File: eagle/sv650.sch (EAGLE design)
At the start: 18 parts, among them IC1 7805

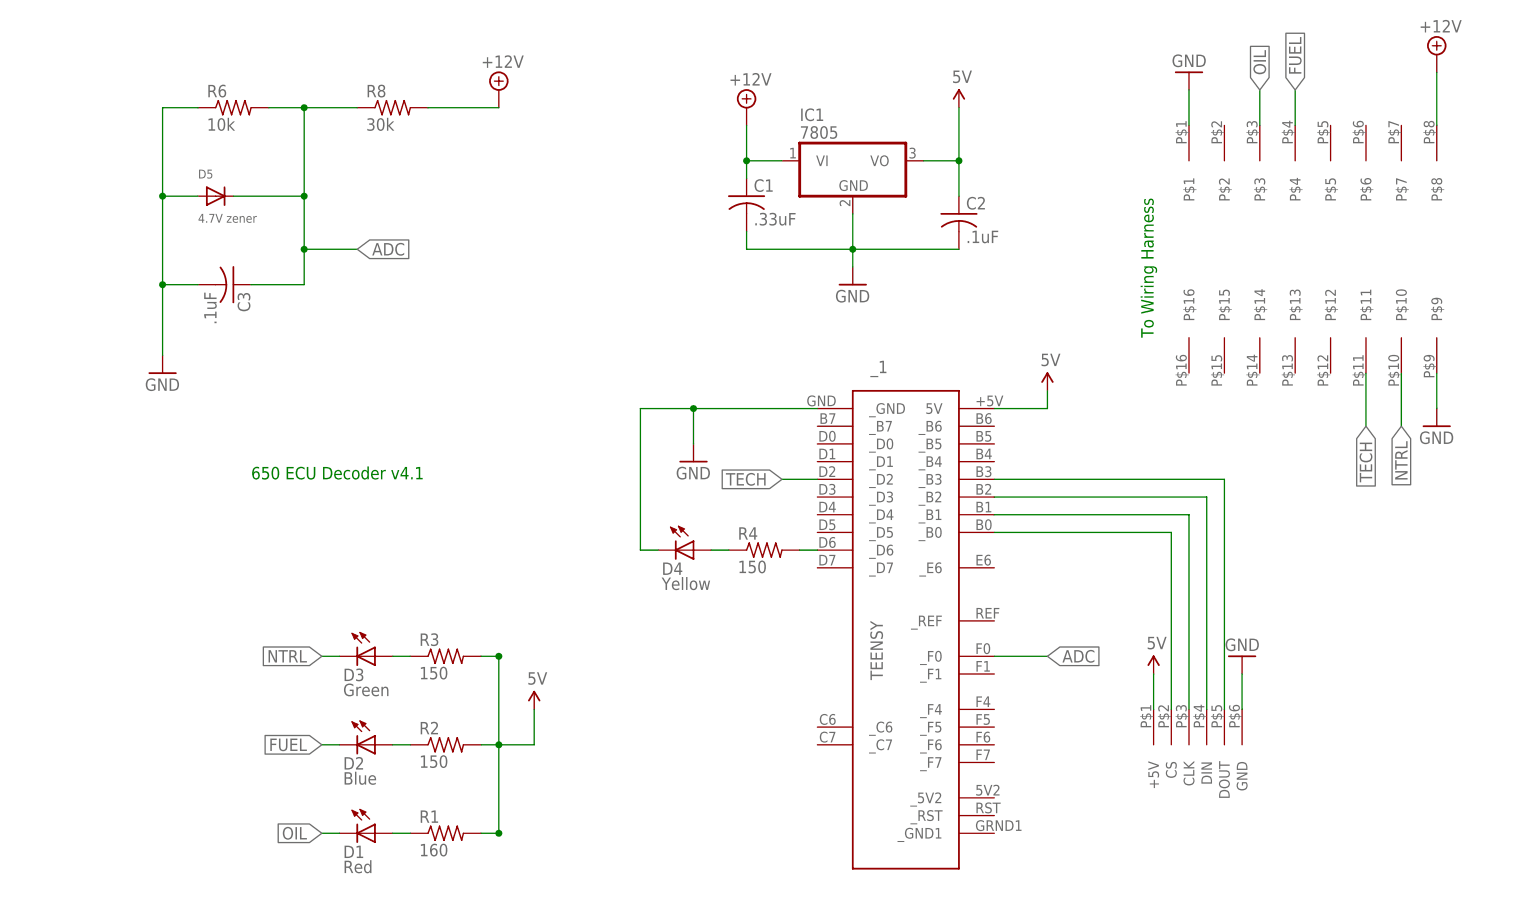
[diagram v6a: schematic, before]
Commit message: Add 'mode' button Add means to detect Very Low Fuel on later models Move +12V back to ignition
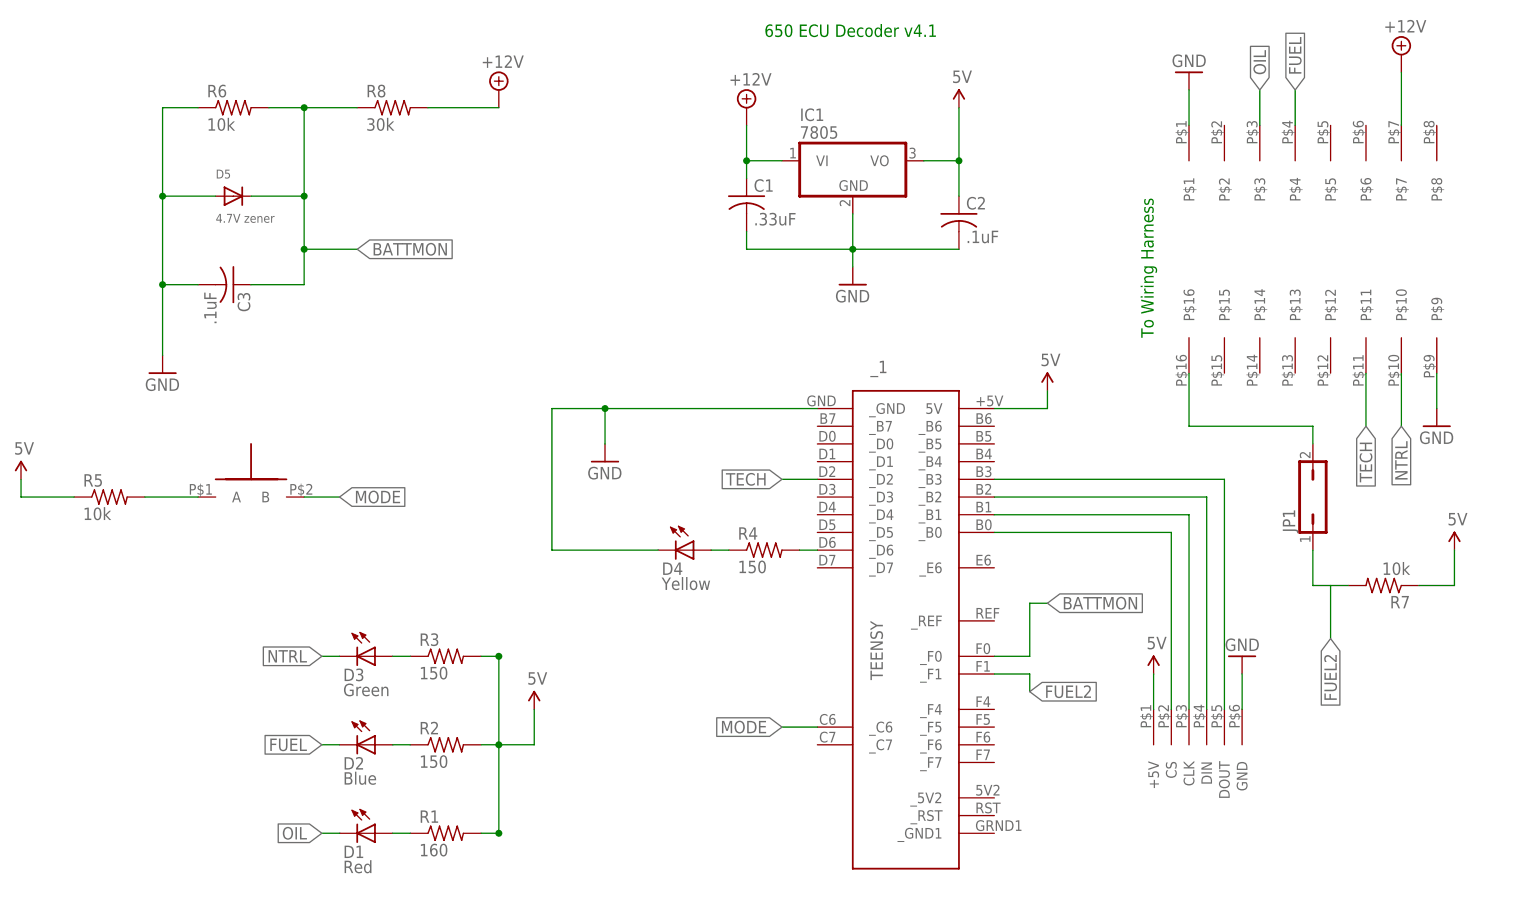
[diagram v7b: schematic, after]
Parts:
- added JP1: (no value), jumper:JP1Q
- added R5, R7: 10k, resistor:R-US_M0805
- added U$10: R13-509A-05-BB/R13-509A-05-BR, synfinatic:R13-509A-05-BB/R13-509A-05-BR
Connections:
- net ADC renamed BATTMON
- new net FUEL2: JP1.1, R7.2, _1._F1
- new net LOWFUEL2: JP1.2, U$3.P$16
- new net MODE: U$10.B, _1._C6
- new net N$12: R5.2, U$10.A
- net +12V: now also U$3.P$7; no longer U$3.P$8
- net 5V: now also R5.1, R7.1
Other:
- moved on the sheet: D5
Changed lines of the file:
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@@
 <attribute name="OC_NEWARK" value="05F1511"/>
 </part>
-<part name="SUPPLY3" library="supply2" deviceset="+12V" device=""/>
 <part name="GND2" library="SparkFun" deviceset="GND" device=""/>
 <part name="C3" library="adafruit" deviceset="C-US" device="025-024X044" value=".1uF">
@@
 <attribute name="OC_NEWARK" value="35K8677"/>
 </part>
+<part name="R5" library="resistor" deviceset="R-US_" device="M0805" value="10k">
+<attribute name="MF" value="VISHAY/DALE"/>
+<attribute name="MPN" value="CRCW080510K0FKTA"/>
+<attribute name="OC_NEWARK" value="05F1511"/>
+</part>
+<part name="U$11" library="SparkFun" deviceset="5V" device=""/>
+<part name="U$10" library="synfinatic" deviceset="R13-509A-05-BB/R13-509A-05-BR" device=""/>
+<part name="SUPPLY4" library="supply2" deviceset="+12V" device=""/>
+<part name="JP1" library="jumper" deviceset="JP1Q" device=""/>
+<part name="R7" library="resistor" deviceset="R-US_" device="M0805" value="10k">
+<attribute name="MF" value="VISHAY/DALE"/>
+<attribute name="MPN" value="CRCW080510K0FKTA"/>
+<attribute name="OC_NEWARK" value="05F1511"/>
+</part>
+<part name="U$12" library="SparkFun" deviceset="5V" device=""/>
 </parts>
 <sheets>
@@
 <plain>
 <text x="114.3" y="68.58" size="1.778" layer="91" rot="R90">To Wiring Harness</text>
-<text x="-15.24" y="48.26" size="1.778" layer="91">650 ECU Decoder v4.1</text>
+<text x="58.42" y="111.76" size="1.778" layer="91">650 ECU Decoder v4.1</text>
 </plain>
 <instances>
@@
 <instance part="GND6" gate="1" x="127" y="22.86" rot="R180"/>
 <instance part="U$9" gate="G$1" x="25.4" y="15.24"/>
-<instance part="GND1" gate="1" x="48.26" y="50.8"/>
+<instance part="GND1" gate="1" x="35.56" y="50.8"/>
 <instance part="SUPPLY1" gate="+12V" x="20.32" y="104.14"/>
 <instance part="SUPPLY2" gate="+12V" x="55.88" y="101.6"/>
@@
 <attribute name="MPN" x="5.08" y="101.6" size="1.778" layer="96" display="off"/>
 </instance>
-<instance part="SUPPLY3" gate="+12V" x="154.94" y="109.22"/>
 <instance part="GND2" gate="1" x="-27.94" y="63.5"/>
 <instance part="C3" gate="G$1" x="-17.78" y="76.2" rot="R270">
@@
 <attribute name="MPN" x="-17.78" y="76.2" size="1.778" layer="96" rot="R270" display="off"/>
 </instance>
-<instance part="D5" gate="G$1" x="-20.32" y="88.9">
-<attribute name="OC_NEWARK" x="-20.32" y="88.9" size="1.778" layer="96" rot="R270" display="off"/>
-<attribute name="MF" x="-20.32" y="88.9" size="1.778" layer="96" rot="R270" display="off"/>
-<attribute name="MPN" x="-20.32" y="88.9" size="1.778" layer="96" rot="R270" display="off"/>
-</instance>
+<instance part="D5" gate="G$1" x="-17.78" y="88.9">
+<attribute name="OC_NEWARK" x="-17.78" y="88.9" size="1.778" layer="96" rot="R270" display="off"/>
+<attribute name="MF" x="-17.78" y="88.9" size="1.778" layer="96" rot="R270" display="off"/>
+<attribute name="MPN" x="-17.78" y="88.9" size="1.778" layer="96" rot="R270" display="off"/>
+</instance>
+<instance part="R5" gate="G$1" x="-35.56" y="45.72">
+<attribute name="OC_NEWARK" x="-35.56" y="45.72" size="1.778" layer="96" display="off"/>
+<attribute name="MF" x="-35.56" y="45.72" size="1.778" layer="96" display="off"/>
+<attribute name="MPN" x="-35.56" y="45.72" size="1.778" layer="96" display="off"/>
+</instance>
+<instance part="U$11" gate="G$1" x="-48.26" y="48.26"/>
+<instance part="U$10" gate="G$1" x="-20.32" y="43.18"/>
+<instance part="SUPPLY4" gate="+12V" x="149.86" y="109.22"/>
+<instance part="JP1" gate="A" x="137.16" y="45.72"/>
+<instance part="R7" gate="G$1" x="147.32" y="33.02" rot="R180">
+<attribute name="OC_NEWARK" x="147.32" y="33.02" size="1.778" layer="96" rot="R180" display="off"/>
+<attribute name="MF" x="147.32" y="33.02" size="1.778" layer="96" rot="R180" display="off"/>
+<attribute name="MPN" x="147.32" y="33.02" size="1.778" layer="96" rot="R180" display="off"/>
+</instance>
+<instance part="U$12" gate="G$1" x="157.48" y="38.1"/>
 </instances>
 <busses>
@@
 <wire x1="114.3" y1="20.32" x2="114.3" y2="15.24" width="0.1524" layer="91"/>
 </segment>
+<segment>
+<pinref part="R5" gate="G$1" pin="1"/>
+<wire x1="-40.64" y1="45.72" x2="-48.26" y2="45.72" width="0.1524" layer="91"/>
+<pinref part="U$11" gate="G$1" pin="5V"/>
+<wire x1="-48.26" y1="45.72" x2="-48.26" y2="48.26" width="0.1524" layer="91"/>
+</segment>
+<segment>
+<pinref part="R7" gate="G$1" pin="1"/>
+<wire x1="152.4" y1="33.02" x2="157.48" y2="33.02" width="0.1524" layer="91"/>
+<wire x1="157.48" y1="33.02" x2="157.48" y2="38.1" width="0.1524" layer="91"/>
+<pinref part="U$12" gate="G$1" pin="5V"/>
+</segment>
 </net>
 <net name="GND" class="0">
@@
 <pinref part="_1" gate="G$1" pin="_GND"/>
 <pinref part="D4" gate="G$1" pin="C"/>
-<wire x1="43.18" y1="38.1" x2="40.64" y2="38.1" width="0.1524" layer="91"/>
-<wire x1="40.64" y1="38.1" x2="40.64" y2="58.42" width="0.1524" layer="91"/>
-<wire x1="40.64" y1="58.42" x2="48.26" y2="58.42" width="0.1524" layer="91"/>
+<wire x1="43.18" y1="38.1" x2="27.94" y2="38.1" width="0.1524" layer="91"/>
+<wire x1="27.94" y1="38.1" x2="27.94" y2="58.42" width="0.1524" layer="91"/>
+<wire x1="27.94" y1="58.42" x2="35.56" y2="58.42" width="0.1524" layer="91"/>
 <pinref part="GND1" gate="1" pin="GND"/>
-<wire x1="48.26" y1="58.42" x2="66.04" y2="58.42" width="0.1524" layer="91"/>
-<wire x1="48.26" y1="53.34" x2="48.26" y2="58.42" width="0.1524" layer="91"/>
-<junction x="48.26" y="58.42"/>
+<wire x1="35.56" y1="58.42" x2="66.04" y2="58.42" width="0.1524" layer="91"/>
+<wire x1="35.56" y1="53.34" x2="35.56" y2="58.42" width="0.1524" layer="91"/>
+<junction x="35.56" y="58.42"/>
 </segment>
 <segment>
@@
 <wire x1="-22.86" y1="101.6" x2="-27.94" y2="101.6" width="0.1524" layer="91"/>
 <wire x1="-27.94" y1="101.6" x2="-27.94" y2="88.9" width="0.1524" layer="91"/>
-<wire x1="-27.94" y1="88.9" x2="-22.86" y2="88.9" width="0.1524" layer="91"/>
+<wire x1="-27.94" y1="88.9" x2="-20.32" y2="88.9" width="0.1524" layer="91"/>
 <wire x1="-27.94" y1="88.9" x2="-27.94" y2="76.2" width="0.1524" layer="91"/>
 <wire x1="-27.94" y1="76.2" x2="-22.86" y2="76.2" width="0.1524" layer="91"/>
@@
 </segment>
 <segment>
-<pinref part="SUPPLY3" gate="+12V" pin="+12V"/>
-<pinref part="U$3" gate="G$1" pin="P$8"/>
-<wire x1="154.94" y1="106.68" x2="154.94" y2="99.06" width="0.1524" layer="91"/>
-</segment>
-</net>
-<net name="ADC" class="0">
+<pinref part="SUPPLY4" gate="+12V" pin="+12V"/>
+<pinref part="U$3" gate="G$1" pin="P$7"/>
+<wire x1="149.86" y1="106.68" x2="149.86" y2="99.06" width="0.1524" layer="91"/>
+</segment>
+</net>
+<net name="BATTMON" class="0">
 <segment>
 <pinref part="_1" gate="G$1" pin="_F0"/>
-<wire x1="91.44" y1="22.86" x2="99.06" y2="22.86" width="0.1524" layer="91"/>
-<label x="99.06" y="22.86" size="1.778" layer="95" xref="yes"/>
+<label x="99.06" y="30.48" size="1.778" layer="95" xref="yes"/>
+<wire x1="91.44" y1="22.86" x2="96.52" y2="22.86" width="0.1524" layer="91"/>
+<wire x1="96.52" y1="22.86" x2="96.52" y2="30.48" width="0.1524" layer="91"/>
+<wire x1="96.52" y1="30.48" x2="99.06" y2="30.48" width="0.1524" layer="91"/>
 </segment>
 <segment>
@@
 <label x="0" y="81.28" size="1.778" layer="95" xref="yes"/>
 <pinref part="R8" gate="G$1" pin="1"/>
-<wire x1="-17.78" y1="88.9" x2="-7.62" y2="88.9" width="0.1524" layer="91"/>
+<wire x1="-15.24" y1="88.9" x2="-7.62" y2="88.9" width="0.1524" layer="91"/>
 <pinref part="R6" gate="G$1" pin="2"/>
 <wire x1="-12.7" y1="101.6" x2="-7.62" y2="101.6" width="0.1524" layer="91"/>
@@
 </segment>
 </net>
+<net name="N$12" class="0">
+<segment>
+<pinref part="R5" gate="G$1" pin="2"/>
+<pinref part="U$10" gate="G$1" pin="A"/>
+<wire x1="-30.48" y1="45.72" x2="-22.86" y2="45.72" width="0.1524" layer="91"/>
+</segment>
+</net>
+<net name="MODE" class="0">
+<segment>
+<pinref part="U$10" gate="G$1" pin="B"/>
+<wire x1="-7.62" y1="45.72" x2="-2.54" y2="45.72" width="0.1524" layer="91"/>
+<label x="-2.54" y="45.72" size="1.778" layer="95" xref="yes"/>
+</segment>
+<segment>
+<pinref part="_1" gate="G$1" pin="_C6"/>
+<wire x1="66.04" y1="12.7" x2="60.96" y2="12.7" width="0.1524" layer="91"/>
+<label x="60.96" y="12.7" size="1.778" layer="95" rot="R180" xref="yes"/>
+</segment>
+</net>
+<net name="LOWFUEL2" class="0">
+<segment>
+<wire x1="119.38" y1="55.88" x2="137.16" y2="55.88" width="0.1524" layer="91"/>
+<pinref part="JP1" gate="A" pin="2"/>
+<wire x1="137.16" y1="55.88" x2="137.16" y2="53.34" width="0.1524" layer="91"/>
+<pinref part="U$3" gate="G$1" pin="P$16"/>
+<wire x1="119.38" y1="63.5" x2="119.38" y2="55.88" width="0.1524" layer="91"/>
+</segment>
+</net>
+<net name="FUEL2" class="0">
+<segment>
+<pinref part="R7" gate="G$1" pin="2"/>
+<wire x1="137.16" y1="33.02" x2="139.7" y2="33.02" width="0.1524" layer="91"/>
+<wire x1="139.7" y1="33.02" x2="142.24" y2="33.02" width="0.1524" layer="91"/>
+<wire x1="139.7" y1="33.02" x2="139.7" y2="25.4" width="0.1524" layer="91"/>
+<label x="139.7" y="25.4" size="1.778" layer="95" rot="R270" xref="yes"/>
+<pinref part="JP1" gate="A" pin="1"/>
+<wire x1="137.16" y1="33.02" x2="137.16" y2="38.1" width="0.1524" layer="91"/>
+</segment>
+<segment>
+<pinref part="_1" gate="G$1" pin="_F1"/>
+<label x="96.52" y="17.78" size="1.778" layer="95" xref="yes"/>
+<wire x1="91.44" y1="20.32" x2="96.52" y2="20.32" width="0.1524" layer="91"/>
+<wire x1="96.52" y1="20.32" x2="96.52" y2="17.78" width="0.1524" layer="91"/>
+</segment>
+</net>

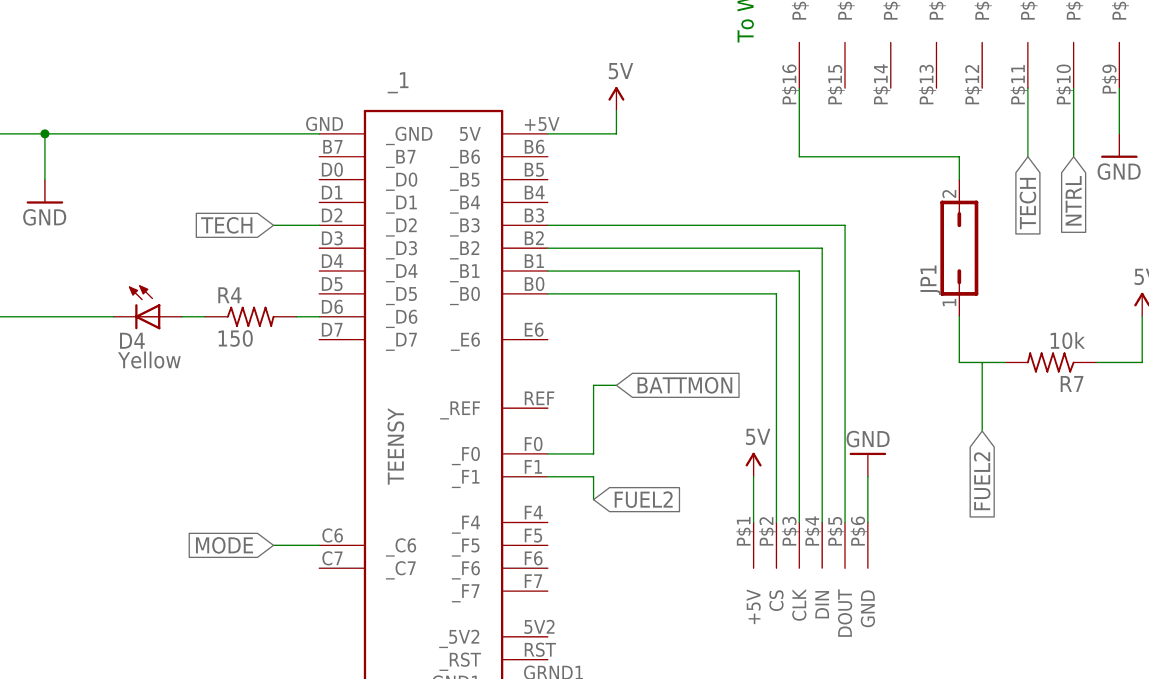
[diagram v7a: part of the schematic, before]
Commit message: Update to v4.2. - Move via away from LM7805 to prevent shorting - Increase size of S/N space
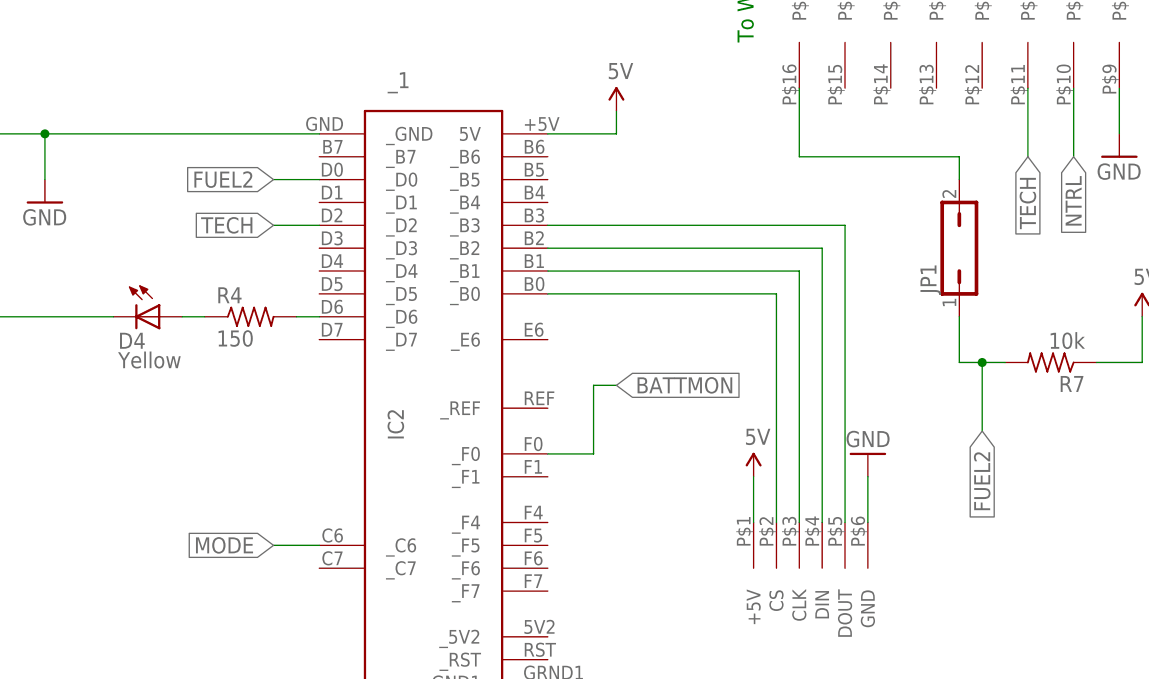
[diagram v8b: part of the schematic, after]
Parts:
- JP1: value (none) -> (none)
- _1: value TEENSY -> IC2
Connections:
- net FUEL2: now also _1._D0; no longer _1._F1
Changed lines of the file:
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@@
 <attribute name="OC_NEWARK" value="unknown"/>
 </part>
-<part name="_1" library="teensy" deviceset="TEENSY" device="">
+<part name="_1" library="teensy" deviceset="TEENSY" device="" value="IC2">
 <attribute name="MF" value=""/>
 <attribute name="MPN" value=""/>
@@
 <part name="U$10" library="synfinatic" deviceset="R13-509A-05-BB/R13-509A-05-BR" device=""/>
 <part name="SUPPLY4" library="supply2" deviceset="+12V" device=""/>
-<part name="JP1" library="jumper" deviceset="JP1Q" device=""/>
+<part name="JP1" library="jumper" deviceset="JP1Q" device="" value=" "/>
 <part name="R7" library="resistor" deviceset="R-US_" device="M0805" value="10k">
 <attribute name="MF" value="VISHAY/DALE"/>
@@
 <pinref part="JP1" gate="A" pin="1"/>
 <wire x1="137.16" y1="33.02" x2="137.16" y2="38.1" width="0.1524" layer="91"/>
-</segment>
-<segment>
-<pinref part="_1" gate="G$1" pin="_F1"/>
-<label x="96.52" y="17.78" size="1.778" layer="95" xref="yes"/>
-<wire x1="91.44" y1="20.32" x2="96.52" y2="20.32" width="0.1524" layer="91"/>
-<wire x1="96.52" y1="20.32" x2="96.52" y2="17.78" width="0.1524" layer="91"/>
-</segment>
-</net>
+<junction x="139.7" y="33.02"/>
+</segment>
+<segment>
+<pinref part="_1" gate="G$1" pin="_D0"/>
+<wire x1="66.04" y1="53.34" x2="60.96" y2="53.34" width="0.1524" layer="91"/>
+<label x="60.96" y="53.34" size="1.778" layer="95" rot="R180" xref="yes"/>
+</segment>
+</net>
